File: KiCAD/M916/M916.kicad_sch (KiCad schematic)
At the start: 13 parts, among them J1 OrangePi ONE, J2 SW-LED, J3 UART, J4 SW-LED, J5 UART, J6 DOOR SW, J7 POWER CHECK RLY, J8 To DGS, J9 To OLT

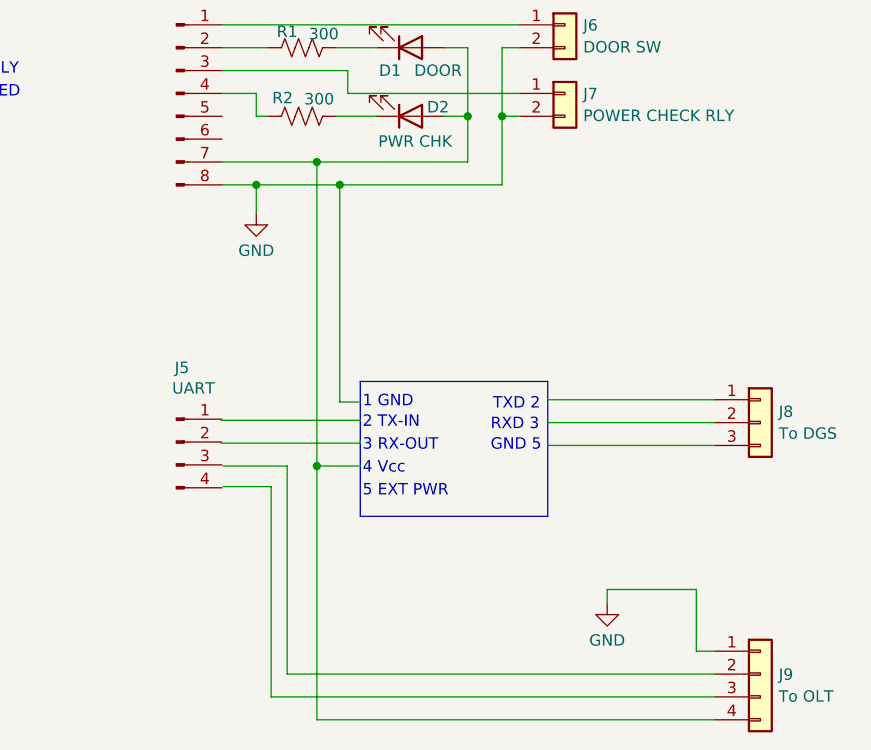
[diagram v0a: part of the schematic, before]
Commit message: ADM3202ライブラリをプライベートに追加
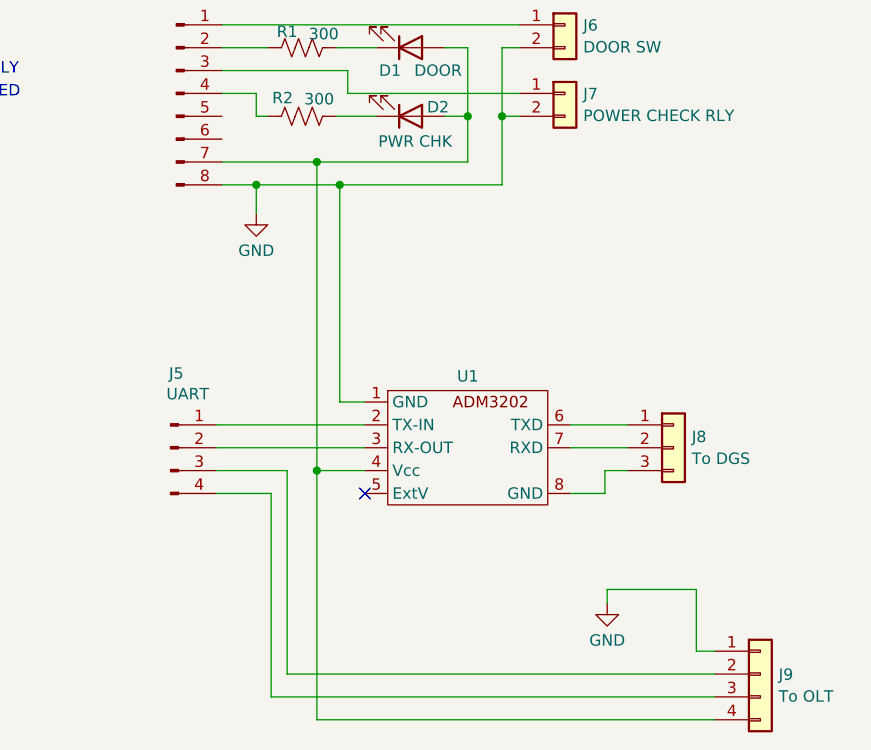
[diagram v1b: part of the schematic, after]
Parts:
- added U1: ~, holly:AE-ADM3202, symbol ae-adm3202:AE-ADM3202
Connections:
- net GND: now also U1.1 (GND)
- net at D1.2 (A), D2.2 (A), J4.7 (Pin_7)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: now also U1.4 (Vcc)
- net at J9.2 (Pin_2): now also J5.3 (Pin_3)
- net at J9.3 (Pin_3): now also J5.4 (Pin_4)
- net at J5.1 (Pin_1): now also U1.2 (TX-IN)
- net at J5.2 (Pin_2): now also U1.3 (RX-OUT)
- net at J8.1 (Pin_1): now also U1.6 (TXD)
- net at J8.2 (Pin_2): now also U1.7 (RXD)
- net at J8.3 (Pin_3): now also U1.8 (GND)
- no-connect marks 0 -> 1
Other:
- note removed: "1 GND"
- note removed: "2 TX-IN"
- note removed: "3 RX-OUT"
- note removed: "4 Vcc"
- note removed: "5 EXT PWR"
- note removed: "GND 5"
- note removed: "RXD 3"
- note removed: "TXD 2"
- moved on the sheet: J5, J8
